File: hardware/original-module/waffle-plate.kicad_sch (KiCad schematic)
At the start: 70 parts, among them P1 J1 L, P10 J21, P11 J22, P12 J24 P1, P13 J25 P1, P14 J27 P, P15 J28 P, P16 J32 (16/15), P17 p23 T1, P18 p25 T4, P19 p5 N0, P2 J4 N, P20 p7 T7, P21 p10 T8, P22 p12 T6, P23 p14 T5, P24 p16 P0, P25 p1 FG5/FG6, P3 J5 N, P4 J7 L1A, P5 J10 (5), P6 J11 (8/7), P7 J14 (12/13), P8 J18 N1, P9 J19 N1, Q1 RJP6012, Q10 RJP6012, Q11 RJP6012, Q12 RJP6012, Q13 RJP6012, Q2 RJP6012, Q3 RJP6012, Q4 NPN (type TBD), Q5 PNP (type TBD), Q6 RJP6012, Q7 RJP6012, Q8 RJP6012, Q9 RJP6012, T1 main transformer 1, T2 main transformer 2

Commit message: Schematic: wire verified input bridge, input shunt and output rectifier
RS1 and RS2 are one shunt in two series parts with Kelvin sense from the
outer terminals (net ties NT1, NT2). RS3 stays unverified.

Co-Authored-By: Claude Opus 5.5 <noreply@anthropic.com>
Claude-Session: https://claude.ai/code/session_01TS5rJ6m2KPqTRFySQXpeEh
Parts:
- removed RS1, RS2: shunt (value TBD), symbol Device:R_Shunt
- added NT1, NT2: Kelvin sense, symbol Device:NetTie_2
- added RS1, RS2: shunt (value TBD), symbol Device:R
- D1, D2, D3, D4: Location_px upper left: (900,420) (1580,450) (870,1280) (1450,1150); ro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 -> upper left: (900,400) (1600,450) (880,1270) (1470,1150); ro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; Verified no -> yes
- D11, D12, D13, D14, D15, D16, D17, D18, D19, D20: Location_px upper right; physical mapping in docs/schematic-notes.md -> upper right; letter mapping in docs/schematic-notes.md; Verified no -> yes
- P1, P19, P2, P20, P21, P22, P23, P24, P3, P4, P5, P6: Verified no -> yes
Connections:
- net ISNS_IN_A: now also NT1.2
- net ISNS_IN_B: now also NT2.2
- net PGND: now also NT2.1, RS2.2
- net VREC-: now also NT1.1, RS1.1
- new net SHUNT_MID: RS1.2, RS2.1
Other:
- note added: "DRAFT. Sections A and D are meter-verified and drawn with wires; the rest uses net labels. Topology is from the community draft schematic plus identified part numbers. Connections are NOT yet verified against the module. Hidden fields per part: Verified, Draft_ref, Location_px (pixel position in images/stitched/waffle-plate-top.jpg)."
- note added: "F. Remaining module pads (draft numbering, unverified)"
- note added: "Kelvin sense taken from the outer terminals (NT1, NT2)."
- note added: "RS1 + RS2: one current shunt in two parts."
- note added: "Verified pads are drawn next to their circuit in A and D."
- note added: "Verified with meter: D11-D20 and pads."
- note removed: "DRAFT. Topology is from the community draft schematic plus identified part numbers. Connections are NOT yet verified against the module. Hidden fields per part: Verified, Draft_ref, Location_px (pixel position in images/stitched/waffle-plate-top.jpg)."
- note removed: "F. Module pads (draft numbering, unverified)"
- note removed: "OUT_P = P0 (battery +), OUT_N = N0 (battery -)"
- note removed: "Outputs are in series. D12 and D13 bypass each bridge."
- note removed: "RS2: function and connections TBD"
- note removed: "Upper bridge D11/D14/D15/D18 rectifies T5-T6; lower bridge D16/D19/D17/D20 rectifies T7-T8."

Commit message: Schematic: wire the PFC stage
Gate driver totem pole, per-IGBT gate resistors, Q1-Q3 in parallel and
boost diodes D5/D6, with pads J14, J18/J19, J21/J22 and J24/J25 drawn
next to the circuit. Netlist unchanged; parts stay unverified pending a
meter check.

Co-Authored-By: Claude Opus 5.5 <noreply@anthropic.com>
Claude-Session: https://claude.ai/code/session_01TS5rJ6m2KPqTRFySQXpeEh
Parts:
- D5, D6: value boost diode (type TBD) -> boost diode, type TBD; Note (none) -> Netlist believed correct; not yet meter-verified
- Q1, Q2, Q3: Note (none) -> Netlist believed correct; not yet meter-verified
- R1, R2, R3: value Rg (value TBD) -> Rg ?; Note (none) -> Netlist believed correct; not yet meter-verified
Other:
- note added: "Netlist believed correct, not yet meter-verified."
- note added: "Pads for A, B and D are drawn next to their circuit."
- note added: "Q1-Q3 in parallel, each with its own gate resistor. D5, D6 in parallel."
- note removed: "Q1-Q3 in parallel. D5, D6 in parallel."
- note removed: "Verified pads are drawn next to their circuit in A and D."

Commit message: Schematic: verified PFC gate driver, add 43R, 1uF and 10k pull-down
Meter checks confirm the emitter-follower wiring read from the image.
Q4/Q5 marked verified; R8 (43R supply), C4 (1uF decoupling) and R4
(10k gate pull-down) added and verified. Docs updated.

Co-Authored-By: Claude Opus 5.5 <noreply@anthropic.com>
Claude-Session: https://claude.ai/code/session_01TS5rJ6m2KPqTRFySQXpeEh
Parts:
- added C4: 1uF, symbol Device:C
- added R4: 10k, symbol Device:R
- added R8: 43, symbol Device:R
- Q4: value NPN (type TBD) -> NPN (BCX56-16 type); Location_px upper left small-signal area ~(1000,2120)? -> centre die (830,2105); Note Gate driver totem pole per draft -> Emitter follower, verified with meter. See docs/pfc-gate-dr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; Verified no -> yes
- Q5: value PNP (type TBD) -> PNP (BCX53-16 type); Location_px upper left small-signal area ~(1250,2050)? -> top-right die (1040,2000); Note Gate driver totem pole per draft -> Emitter follower, verified with meter. See docs/pfc-gate-dr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; Verified no -> yes
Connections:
- net PFC_GDRV: now also R4.1
- net PGND: now also C4.2, R4.2
- net VDRV: now also R8.1; no longer Q4.3 (C)
- new net VDRV_F: C4.1, Q4.3 (C), R8.2
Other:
- note added: "Gate driver (Q4, Q5, R4, R8, C4) meter-verified. IGBTs, gate resistors and boost diodes believed correct, not yet meter-verified."
- note removed: "Netlist believed correct, not yet meter-verified."

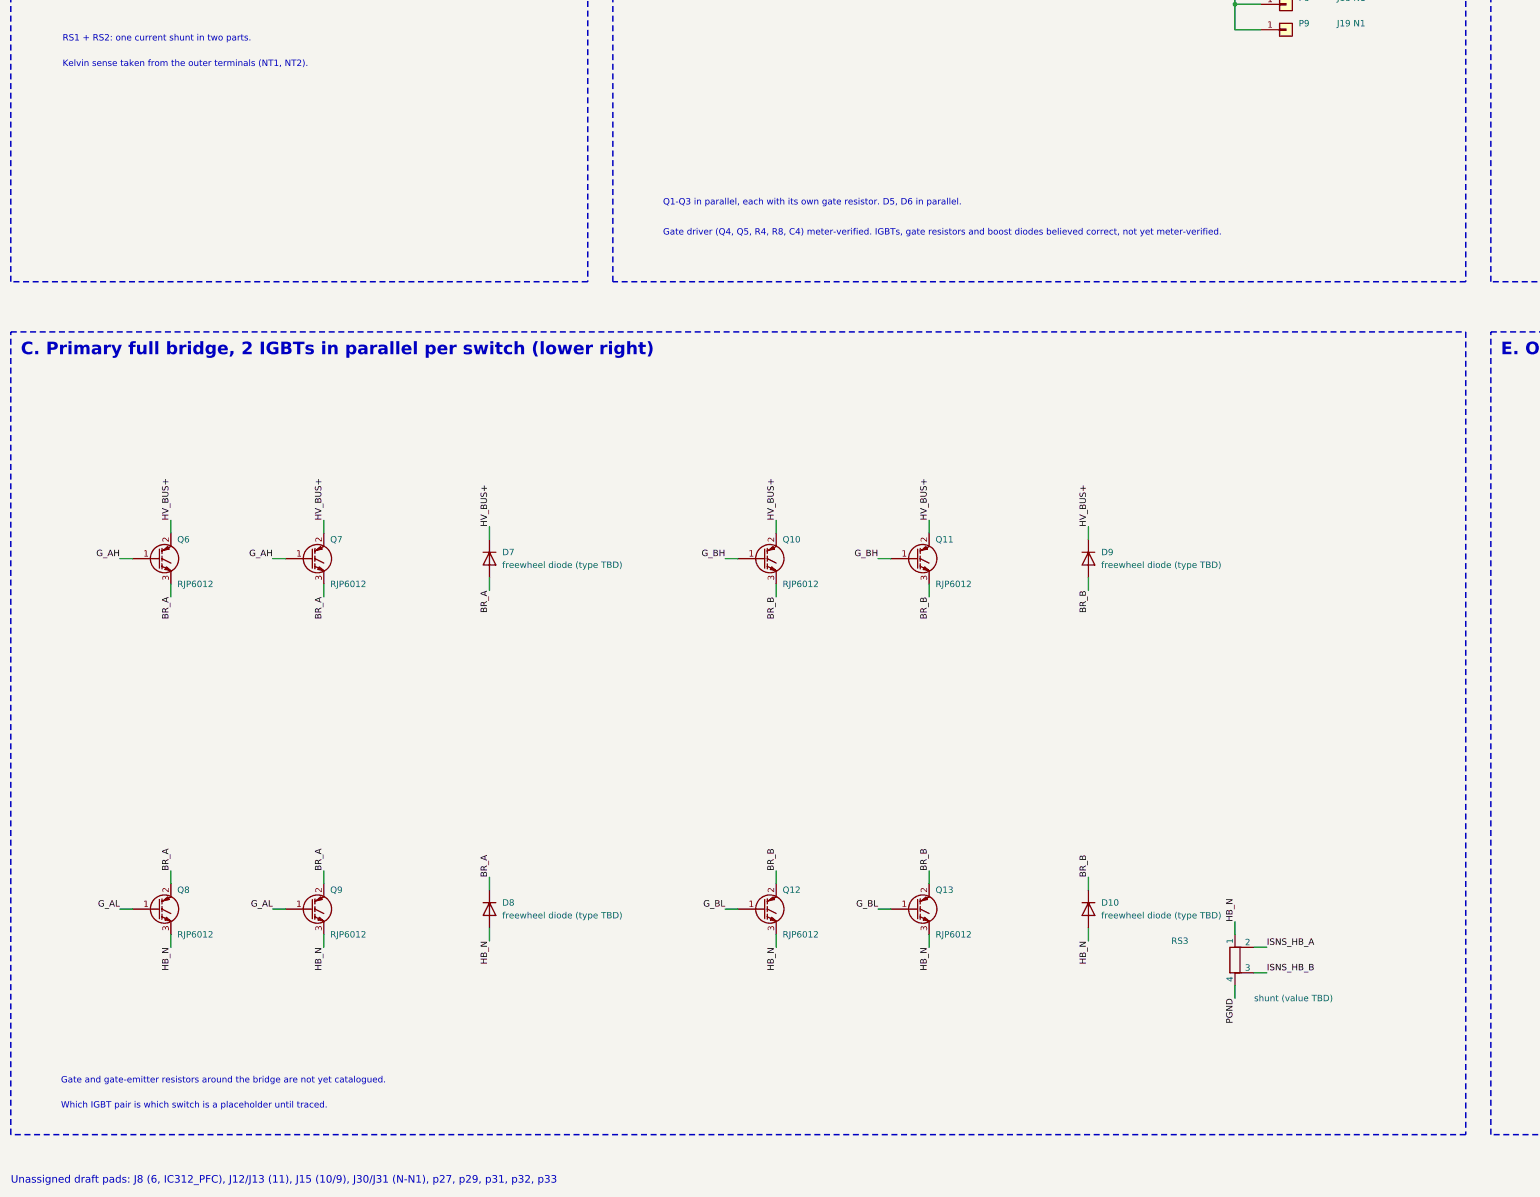
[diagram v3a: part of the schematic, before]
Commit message: Schematic: add full-bridge gate networks (unconfirmed)
Section C now has each switch's six-part gate network (Rg1, Rg2, Rgg,
C1, C2, Rge) with separate drive-input and gate nets, using reference
values marked '?'. BH/BL traced from copper; AH/AL by analogy. RS3 moved
to section A for space. Docs: Angel's design matches the traced
topology; values checked against stand-in datasheets (RJP60V0DPM,
HGTG10N120BND); AL failure and gate-termination damage noted.

Co-Authored-By: Claude Opus 5.5 <noreply@anthropic.com>
Claude-Session: https://claude.ai/code/session_01TS5rJ6m2KPqTRFySQXpeEh
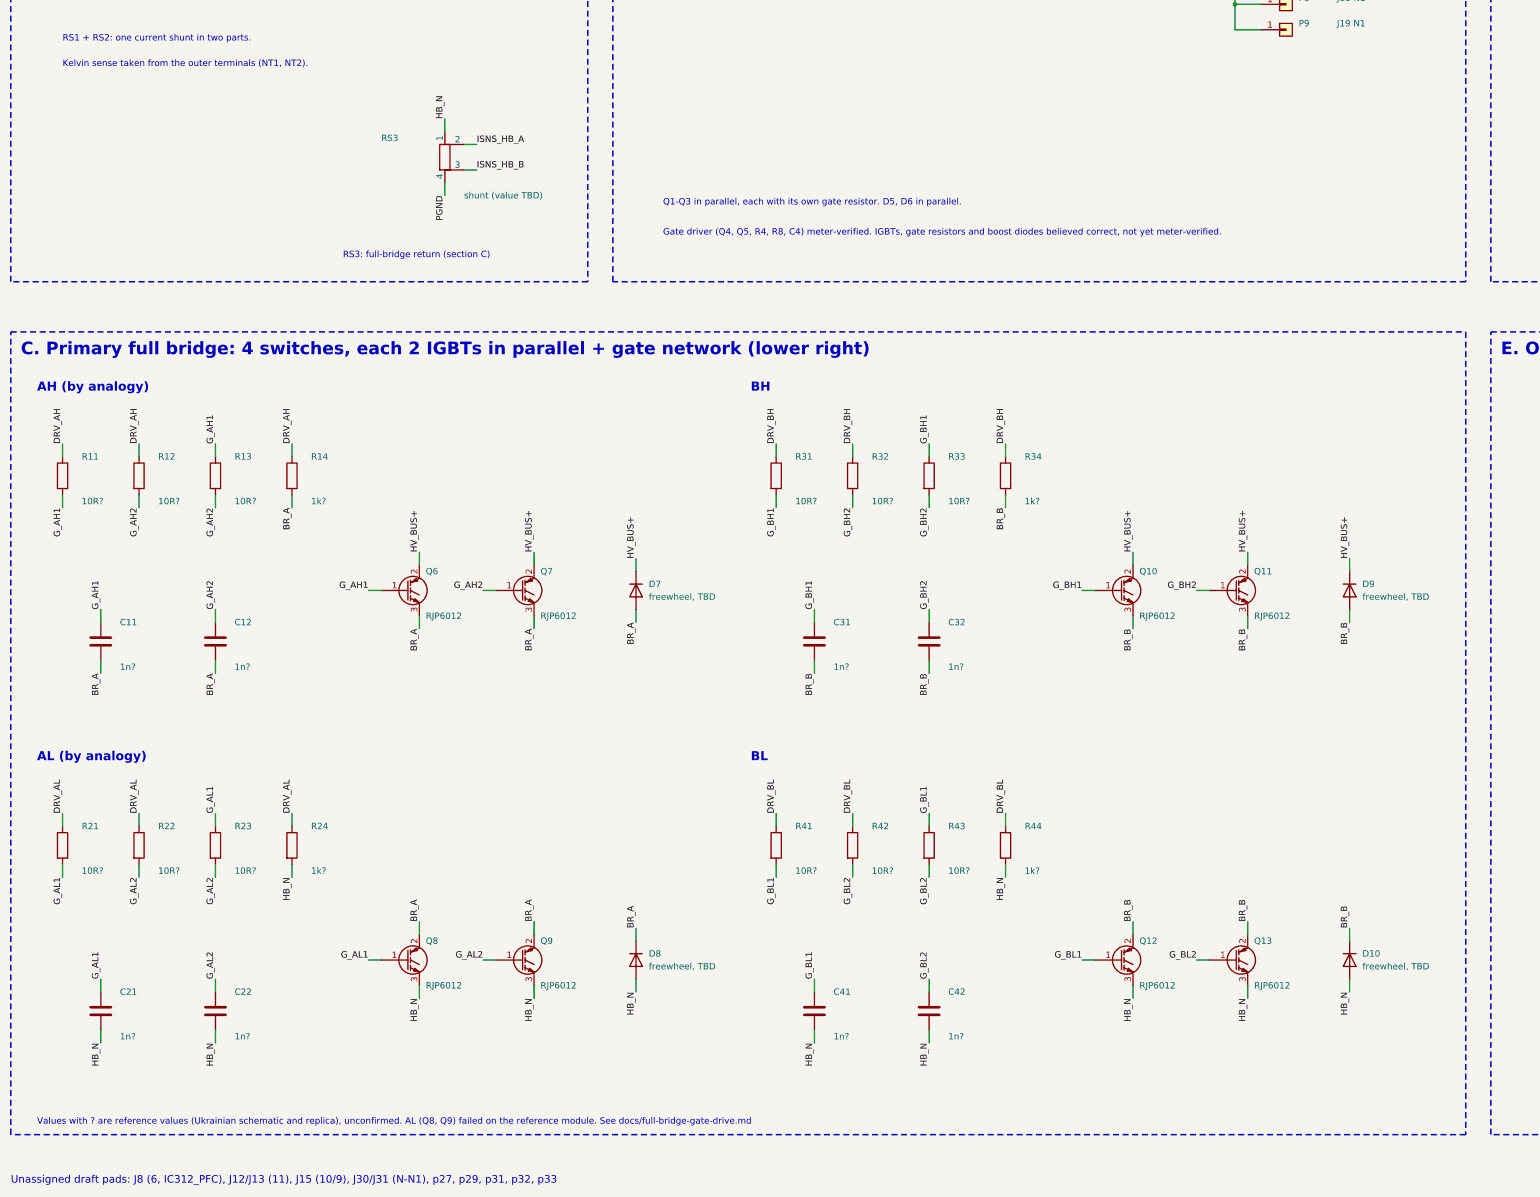
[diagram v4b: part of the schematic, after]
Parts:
- added C11, C12, C21, C22, C31, C32, C41, C42: 1n?, symbol Device:C
- added R11, R12, R13, R21, R22, R23, R31, R32, R33, R41, R42, R43: 10R?, symbol Device:R
- added R14, R24, R34, R44: 1k?, symbol Device:R
- D10: value freewheel diode (type TBD) -> freewheel, TBD; Location_px bottom-right group (3400,4050) (3900,4050), diode (4350,404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 -> (4350,4040); Note Antiparallel diode, switch B low -> Antiparallel diode, switch BL. Both outer leads bonded to t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
- D7: value freewheel diode (type TBD) -> freewheel, TBD; Location_px top-left group (2600,3370) (3100,3370), diode (2200,3340) -> (2200,3340); Note Antiparallel diode, switch A high -> Antiparallel diode, switch AH. Both outer leads bonded to t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
- D8: value freewheel diode (type TBD) -> freewheel, TBD; Location_px bottom-left group (2370,4100) (2830,4100), diode (1990,4120) -> (1990,4120); Note Antiparallel diode, switch A low -> Antiparallel diode, switch AL. Both outer leads bonded to t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
- D9: value freewheel diode (type TBD) -> freewheel, TBD; Location_px top-right group (3600,3200) (4100,3200), diode (4520,3240) -> (4520,3240); Note Antiparallel diode, switch B high -> Antiparallel diode, switch BH. Both outer leads bonded to t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
- Q10: Location_px top-right group (3600,3200) (4100,3200), diode (4520,3240) -> (3600,3200); Note Switch B high; group-to-switch assignment TBD -> Switch BH, IGBT 1.
- Q11: Location_px top-right group (3600,3200) (4100,3200), diode (4520,3240) -> (4100,3200); Note Switch B high; group-to-switch assignment TBD -> Switch BH, IGBT 2.
- Q12: Location_px bottom-right group (3400,4050) (3900,4050), diode (4350,404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 -> (3400,4050); Note Switch B low; group-to-switch assignment TBD -> Switch BL, IGBT 1.
- Q13: Location_px bottom-right group (3400,4050) (3900,4050), diode (4350,404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 -> (3900,4050); Note Switch B low; group-to-switch assignment TBD -> Switch BL, IGBT 2.
- Q6: Location_px top-left group (2600,3370) (3100,3370), diode (2200,3340) -> (2600,3370); Note Switch A high; group-to-switch assignment TBD -> Switch AH, IGBT 1.
- Q7: Location_px top-left group (2600,3370) (3100,3370), diode (2200,3340) -> (3100,3370); Note Switch A high; group-to-switch assignment TBD -> Switch AH, IGBT 2.
- Q8: Location_px bottom-left group (2370,4100) (2830,4100), diode (1990,4120) -> (2370,4100); Note Switch A low; group-to-switch assignment TBD -> Switch AL, IGBT 1. FAILED/RUPTURED on the reference module;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
- Q9: Location_px bottom-left group (2370,4100) (2830,4100), diode (1990,4120) -> (2830,4100); Note Switch A low; group-to-switch assignment TBD -> Switch AL, IGBT 2. FAILED/RUPTURED on the reference module;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
- RS3: Draft_ref R? at J30-J32 (N-N1, 16/15) -> R? at J30-J32 (N-N1, 16/15); R16 0R in Ukr. schematic; Note Full-bridge return current shunt -> Full-bridge return. Possibly a 0 ohm link rather than a shu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
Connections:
- net BR_A: now also C11.2, C12.2, R14.2
- net BR_B: now also C31.2, C32.2, R34.2
- net HB_N: now also C21.2, C22.2, C41.2, C42.2, R24.2, R44.2
- net G_AH renamed G_AH1
- net G_AH1: now also C11.1, R11.2, R13.1; no longer Q7.1 (G)
- net G_AL renamed G_AL1
- net G_AL1: now also C21.1, R21.2, R23.1; no longer Q9.1 (G)
- net G_BH renamed G_BH1
- net G_BH1: now also C31.1, R31.2, R33.1; no longer Q11.1 (G)
- net G_BL renamed G_BL1
- net G_BL1: now also C41.1, R41.2, R43.1; no longer Q13.1 (G)
- new net DRV_AH: R11.1, R12.1, R14.1
- new net DRV_AL: R21.1, R22.1, R24.1
- new net DRV_BH: R31.1, R32.1, R34.1
- new net DRV_BL: R41.1, R42.1, R44.1
- new net G_AH2: C12.1, Q7.1 (G), R12.2, R13.2
- new net G_AL2: C22.1, Q9.1 (G), R22.2, R23.2
- new net G_BH2: C32.1, Q11.1 (G), R32.2, R33.2
- new net G_BL2: C42.1, Q13.1 (G), R42.2, R43.2
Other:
- note added: "AH (by analogy)"
- note added: "AL (by analogy)"
- note added: "BH"
- note added: "BL"
- note added: "C. Primary full bridge: 4 switches, each 2 IGBTs in parallel + gate network (lower right)"
- note added: "RS3: full-bridge return (section C)"
- note added: "Values with ? are reference values (Ukrainian schematic and replica), unconfirmed. AL (Q8, Q9) failed on the reference module. See docs/full-bridge-gate-drive.md"
- note removed: "C. Primary full bridge, 2 IGBTs in parallel per switch (lower right)"
- note removed: "Gate and gate-emitter resistors around the bridge are not yet catalogued."
- note removed: "Which IGBT pair is which switch is a placeholder until traced."
